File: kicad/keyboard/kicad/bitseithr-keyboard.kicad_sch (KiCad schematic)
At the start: 74 parts, among them P2 KEYB CONN 1

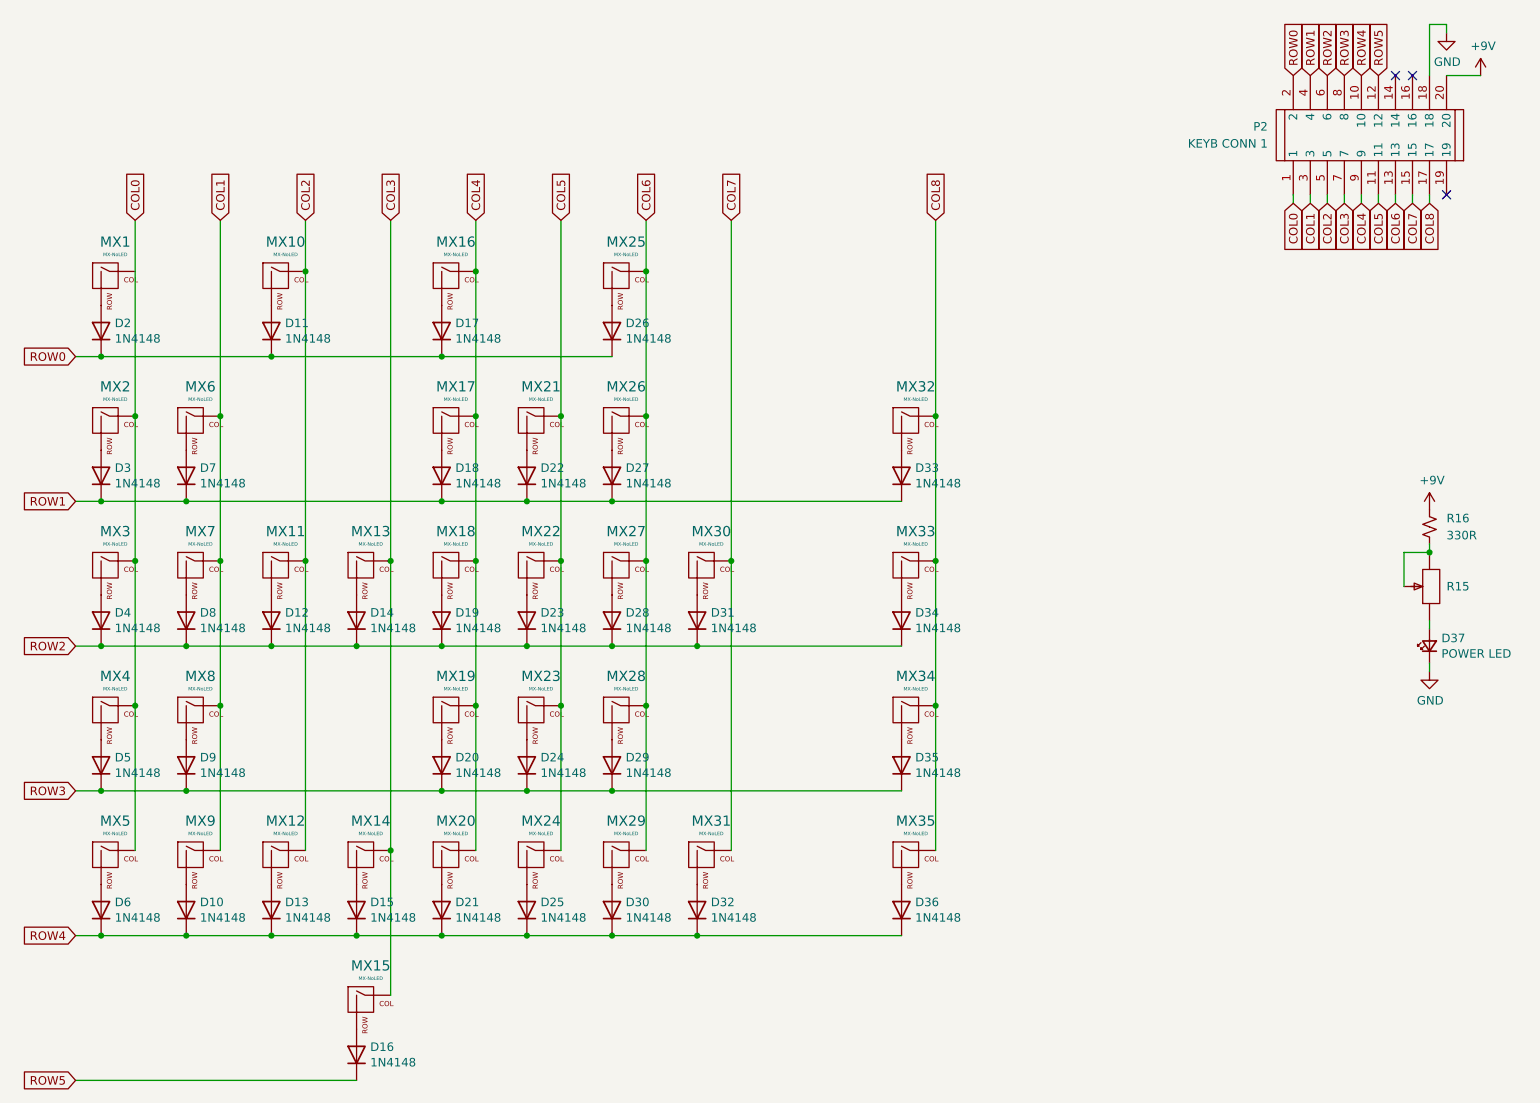
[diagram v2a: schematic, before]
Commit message: updated keyboard connector pinout again for better routing
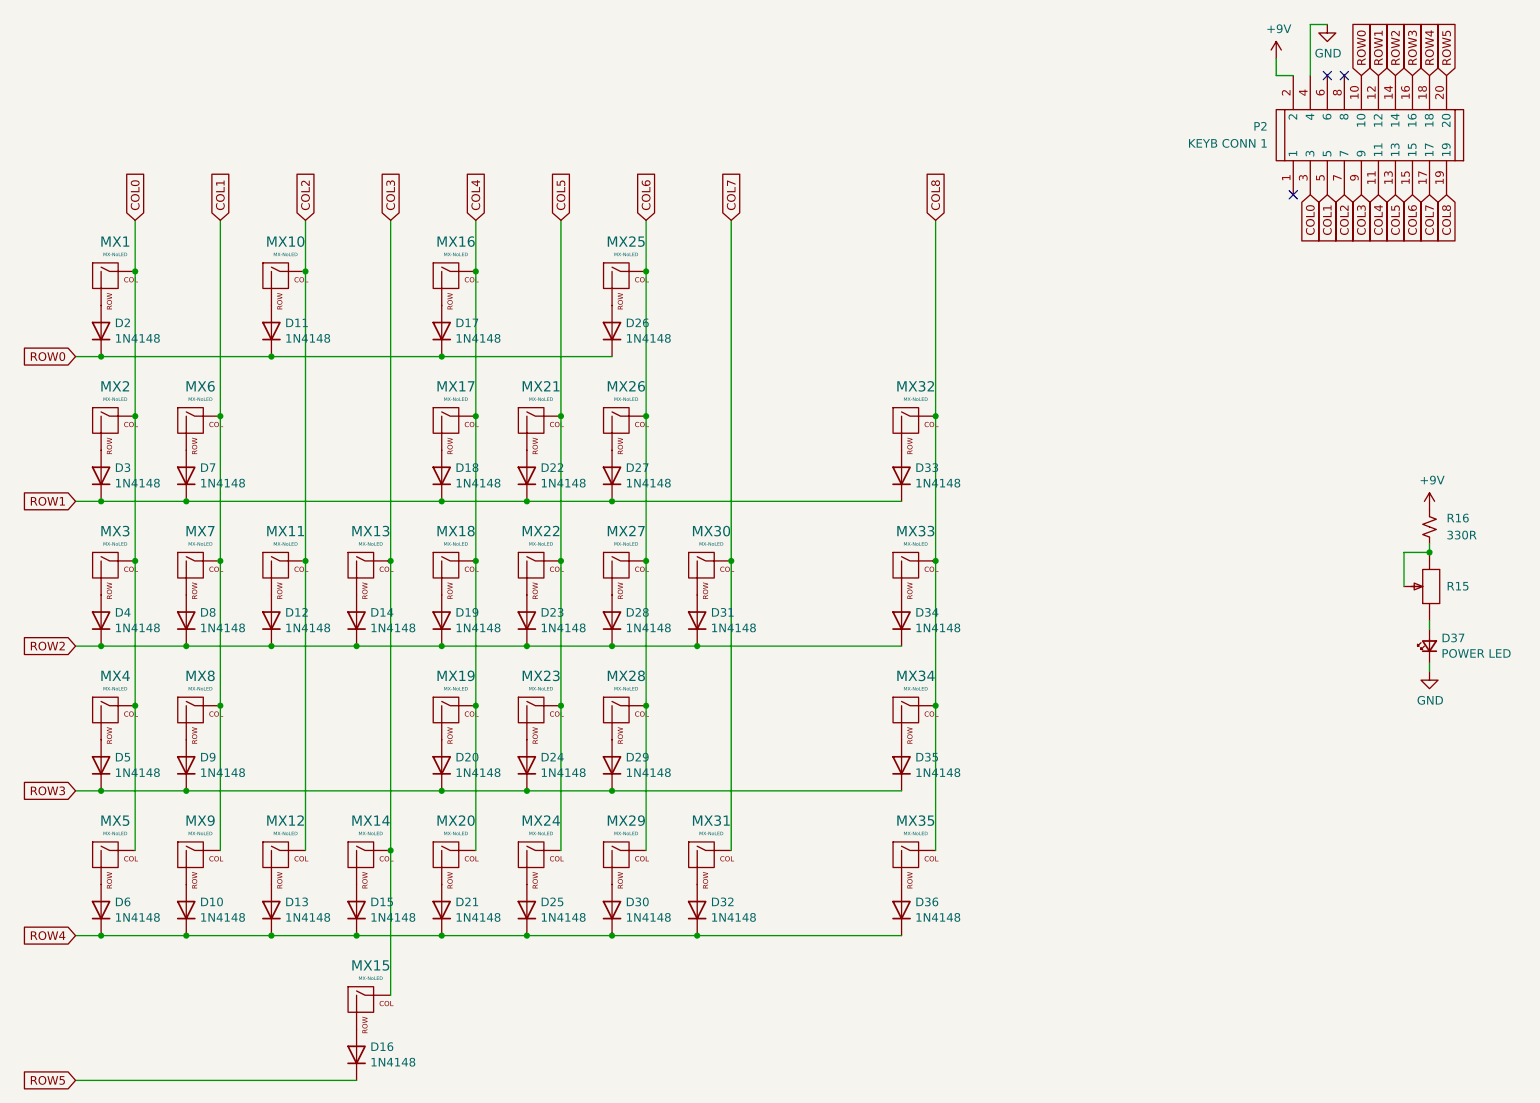
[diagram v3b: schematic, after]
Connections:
- net +9V: now also P2.2; no longer P2.20
- net COL0: now also MX1.1 (COL), P2.3; no longer P2.1
- net COL1: now also P2.5; no longer P2.3
- net COL2: now also P2.7; no longer P2.5
- net COL3: now also P2.9; no longer P2.7
- net COL4: now also P2.11; no longer P2.9
- net COL5: now also P2.13; no longer P2.11
- net COL6: now also P2.15; no longer P2.13
- net COL7: now also P2.17; no longer P2.15
- net COL8: now also P2.19; no longer P2.17
- net GND: now also P2.4; no longer P2.18
- net ROW0: now also P2.10; no longer P2.2
- net ROW1: now also P2.12; no longer P2.4
- net ROW2: now also P2.14; no longer P2.6
- net ROW3: now also P2.16; no longer P2.8
- net ROW4: now also P2.18; no longer P2.10
- net ROW5: now also P2.20; no longer P2.12
